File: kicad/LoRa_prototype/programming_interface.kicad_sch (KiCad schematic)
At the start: 1 part, among them J1 Conn_ST_STDC14

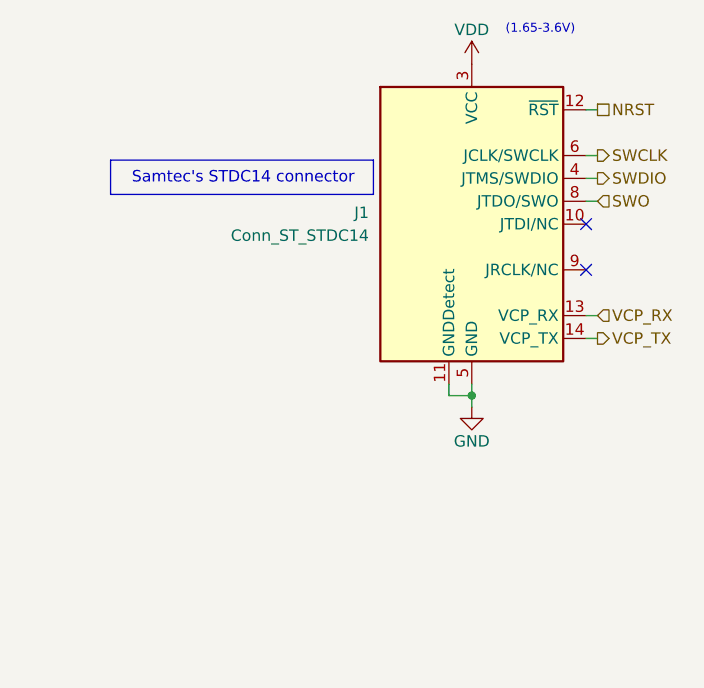
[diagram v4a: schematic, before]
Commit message: Added footprints SPV1050 & SPI Flash
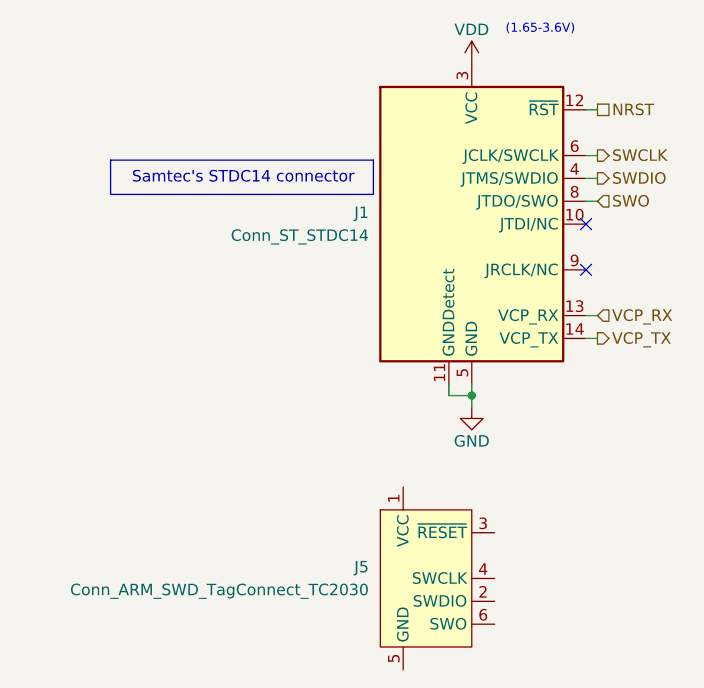
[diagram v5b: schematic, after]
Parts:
- added J5: Conn_ARM_SWD_TagConnect_TC2030, Connector:Tag-Connect_TC2030-IDC-FP_2x03_P1.27mm_Vertical, symbol Connector:Conn_ARM_SWD_TagConnect_TC2030
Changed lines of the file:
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@@
+	)
+	(symbol
+		(lib_id "Connector:Conn_ARM_SWD_TagConnect_TC2030")
+		(at 95.25 102.87 0)
+		(unit 1)
+		(exclude_from_sim no)
+		(in_bom no)
+		(on_board yes)
+		(dnp no)
+		(fields_autoplaced yes)
+		(property "Reference" "J5"
+			(at 88.9 101.5999 0)
+			(effects
+				(font
+					(size 1.27 1.27)
+				)
+				(justify right)
+			)
+		)
+		(property "Value" "Conn_ARM_SWD_TagConnect_TC2030"
+			(at 88.9 104.1399 0)
+			(effects
+				(font
+					(size 1.27 1.27)
+				)
+				(justify right)
+			)
+		)
+		(property "Footprint" "Connector:Tag-Connect_TC2030-IDC-FP_2x03_P1.27mm_Vertical"
+			(at 95.25 120.65 0)
+			(effects
+				(font
+					(size 1.27 1.27)
+				)
+				(hide yes)
+			)
+		)
+		(property "Datasheet" "https://www.tag-connect.com/wp-content/uploads/bsk-pdf-manager/TC2030-CTX_1.pdf"
+			(at 95.25 118.11 0)
+			(effects
+				(font
+					(size 1.27 1.27)
+				)
+				(hide yes)
+			)
+		)
+		(property "Description" "Tag-Connect ARM Cortex SWD JTAG connector, 6 pin"
+			(at 95.25 102.87 0)
+			(effects
+				(font
+					(size 1.27 1.27)
+				)
+				(hide yes)
+			)
+		)
+		(pin "1"
+		)
+		(pin "3"
+		)
+		(pin "4"
+		)
+		(pin "6"
+		)
+		(pin "5"
+		)
+		(pin "2"
+		)
+		(instances
+			(project ""
+				(path "/9fad4700-f514-47ad-821a-b4076ecc08de/90bf3950-abae-4ac1-9a2d-ebd17dec7caa"
+					(reference "J5")
+					(unit 1)
+				)
+			)
+		)
 	)
 	(symbol

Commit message: Done schematic with 0 ERC errors (Milestone)
Still need to double/triple check tho
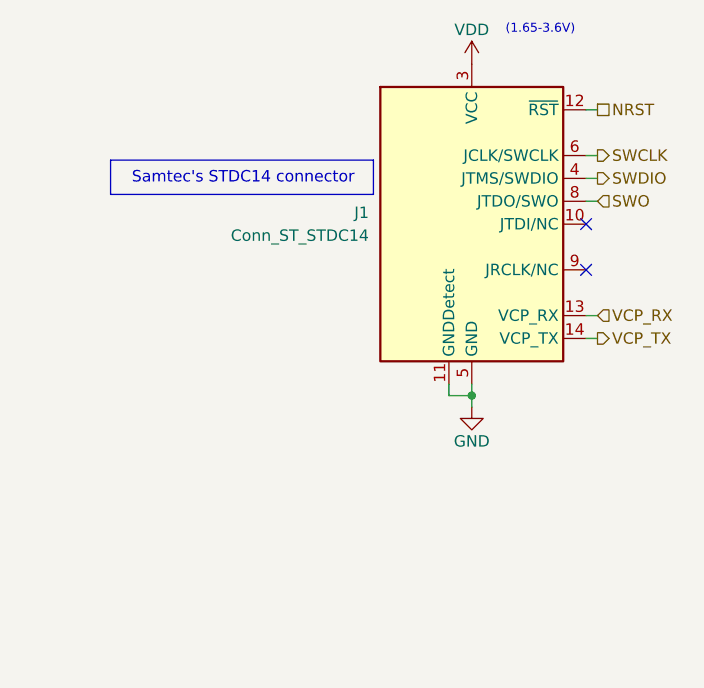
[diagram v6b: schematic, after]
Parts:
- removed J5: Conn_ARM_SWD_TagConnect_TC2030, Connector:Tag-Connect_TC2030-IDC-FP_2x03_P1.27mm_Vertical, symbol Connector:Conn_ARM_SWD_TagConnect_TC2030
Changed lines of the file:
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@@
-	)
-	(symbol
-		(lib_id "Connector:Conn_ARM_SWD_TagConnect_TC2030")
-		(at 95.25 102.87 0)
-		(unit 1)
-		(exclude_from_sim no)
-		(in_bom no)
-		(on_board yes)
-		(dnp no)
-		(fields_autoplaced yes)
-		(property "Reference" "J5"
-			(at 88.9 101.5999 0)
-			(effects
-				(font
-					(size 1.27 1.27)
-				)
-				(justify right)
-			)
-		)
-		(property "Value" "Conn_ARM_SWD_TagConnect_TC2030"
-			(at 88.9 104.1399 0)
-			(effects
-				(font
-					(size 1.27 1.27)
-				)
-				(justify right)
-			)
-		)
-		(property "Footprint" "Connector:Tag-Connect_TC2030-IDC-FP_2x03_P1.27mm_Vertical"
-			(at 95.25 120.65 0)
-			(effects
-				(font
-					(size 1.27 1.27)
-				)
-				(hide yes)
-			)
-		)
-		(property "Datasheet" "https://www.tag-connect.com/wp-content/uploads/bsk-pdf-manager/TC2030-CTX_1.pdf"
-			(at 95.25 118.11 0)
-			(effects
-				(font
-					(size 1.27 1.27)
-				)
-				(hide yes)
-			)
-		)
-		(property "Description" "Tag-Connect ARM Cortex SWD JTAG connector, 6 pin"
-			(at 95.25 102.87 0)
-			(effects
-				(font
-					(size 1.27 1.27)
-				)
-				(hide yes)
-			)
-		)
-		(pin "1"
-		)
-		(pin "3"
-		)
-		(pin "4"
-		)
-		(pin "6"
-		)
-		(pin "5"
-		)
-		(pin "2"
-		)
-		(instances
-			(project ""
-				(path "/9fad4700-f514-47ad-821a-b4076ecc08de/90bf3950-abae-4ac1-9a2d-ebd17dec7caa"
-					(reference "J5")
-					(unit 1)
-				)
-			)
-		)
 	)
 	(symbol
